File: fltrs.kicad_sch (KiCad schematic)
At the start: 55 parts, among them U3 CPC1117N, U4 MCP6002, U5 MCP4451-503-ST, U6 MCP6002, U7 MCP6002

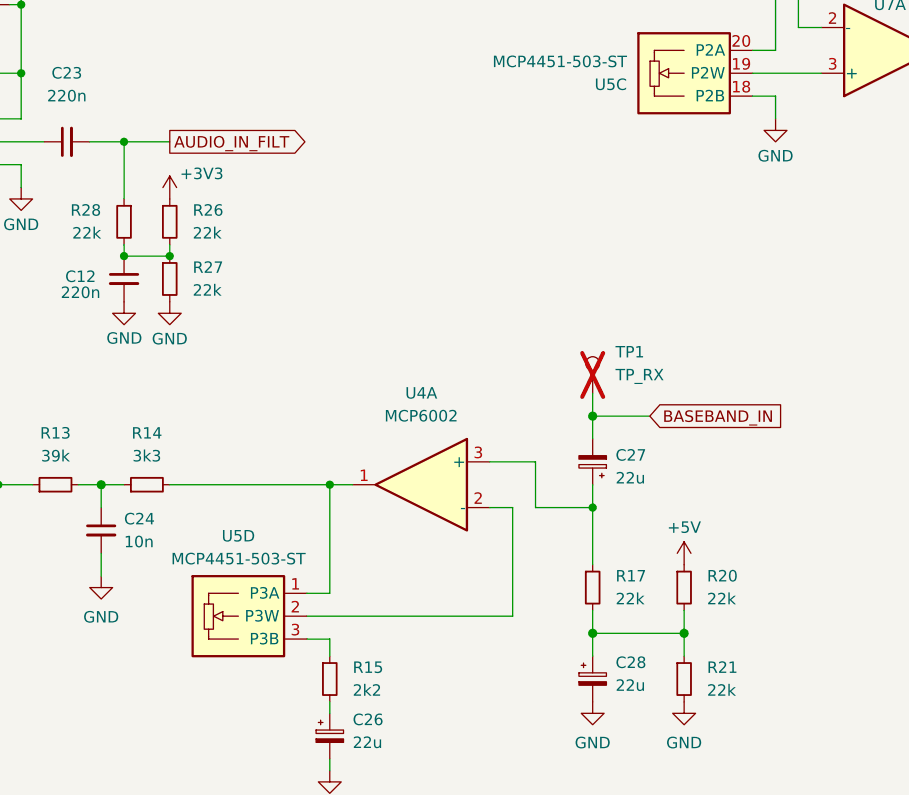
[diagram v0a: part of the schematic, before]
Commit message: Bias voltage changed, usart rx tp add
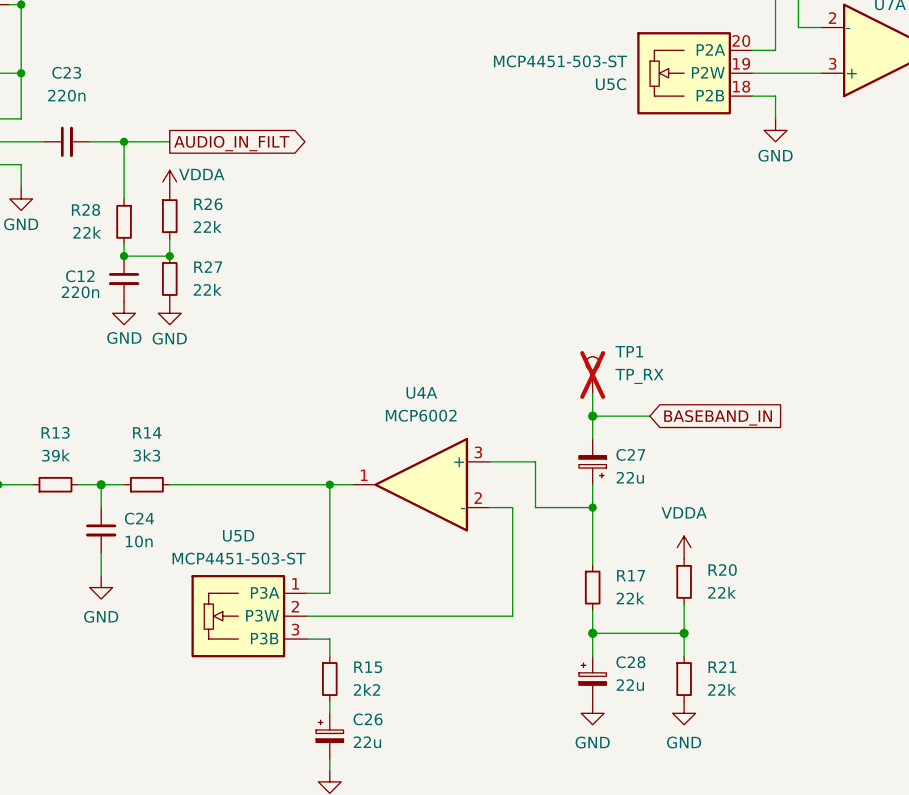
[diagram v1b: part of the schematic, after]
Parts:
- C12, C22, C23: MPN (none) -> C192432
- C14, C15, C16, C19, C20, C29, C31: MPN (none) -> C60133
- C17, C18: MPN (none) -> C284989
- C21, C32: MPN (none) -> C1541
- C24: MPN Generic C/10nF/C0G/25V/0603 -> C60133
- C25, C30, C33, C35: MPN (none) -> C56392
- C26, C27, C28: MPN T491A226K006AT -> C118989
- C34: MPN (none) -> C118989
- R10, R11: MPN (none) -> C2960875
- R12: MPN (none) -> C3015806
- R13: MPN Generic R/39k/0603 -> C25783
- R14: MPN Generic R/3k3/0603 -> C25890
- R15: MPN Generic R/2k2/0603 -> C102890
- R16: MPN (none) -> C102749
- R17, R20, R21, R26, R27, R28: MPN Generic R/22k/0603 -> C2909337
- R18, R19, R22: MPN (none) -> C25890
- R23: MPN (none) -> C25783
- R24: MPN (none) -> C23018
- R25, U3: now left out of the parts list
- R6, R7: MPN (none) -> C25899
- R8, R9: MPN (none) -> C25754
- U4, U6, U7: MPN (none) -> C623660
- U5: MPN (none) -> C627257
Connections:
- net +3V3: no longer R26.1
- net +5V: no longer R20.1
- new net VDDA: R20.1, R26.1
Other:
- moved on the sheet: R20, R26
